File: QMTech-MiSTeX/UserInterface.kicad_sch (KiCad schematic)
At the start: 38 parts, among them CN2 U.FL-R-SMT-1(80), CN3 U.FL-R-SMT-1(80), CN4 U.FL-R-SMT-1(80), SW1 TS-1187A-B-A-B, SW2 TS-1187A-B-A-B, SW3 TS-1187A-B-A-B, SW4 TS-1187A-B-A-B, U6 HX 0.5-24P XGXJ-H2.0

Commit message: QMTech-MiSTeX WIP
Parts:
- removed U6: HX 0.5-24P XGXJ-H2.0, easyeda2kicad:CONN-SMD_24P-P0.50_HANXIA_HX0.5-24PXGXJ-H2.0, symbol easyeda2kicad:HX0.5-24PXGXJ-H2.0
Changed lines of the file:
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@@
-    )
-  )
-  (symbol (lib_id "easyeda2kicad:HX0.5-24PXGXJ-H2.0") (at 148.2598 107.5182 0) (unit 1)
-    (in_bom yes) (on_board yes) (dnp no) (fields_autoplaced)
-    (property "Reference" "U6" (at 156.5148 105.0361 0)
-      (effects (font (size 1.27 1.27)) (justify left))
-    )
-    (property "Value" "HX 0.5-24P XGXJ-H2.0" (at 156.5148 107.4603 0)
-      (effects (font (size 1.27 1.27)) (justify left))
-    )
-    (property "Footprint" "easyeda2kicad:CONN-SMD_24P-P0.50_HANXIA_HX0.5-24PXGXJ-H2.0" (at 148.2598 148.1582 0)
-      (effects (font (size 1.27 1.27)) hide)
-    )
-    (property "Datasheet" "" (at 148.2598 107.5182 0)
-      (effects (font (size 1.27 1.27)) hide)
-    )
-    (property "LCSC Part" "C5142050" (at 148.2598 150.6982 0)
-      (effects (font (size 1.27 1.27)) hide)
-    )
-    (pin "3")
-    (pin "26")
-    (pin "24")
-    (pin "8")
-    (pin "4")
-    (pin "7")
-    (pin "15")
-    (pin "14")
-    (pin "12")
-    (pin "13")
-    (pin "11")
-    (pin "6")
-    (pin "19")
-    (pin "9")
-    (pin "1")
-    (pin "10")
-    (pin "2")
-    (pin "22")
-    (pin "16")
-    (pin "21")
-    (pin "18")
-    (pin "20")
-    (pin "5")
-    (pin "23")
-    (pin "17")
-    (pin "25")
-    (instances
-      (project "QMTech-MiSTeX"
-        (path "/bf95850e-2fcb-4784-a603-f17fc357556b/cce2b405-ae09-44af-ba42-d113d6ffe521"
-          (reference "U6") (unit 1)
-        )
-      )
     )
   )

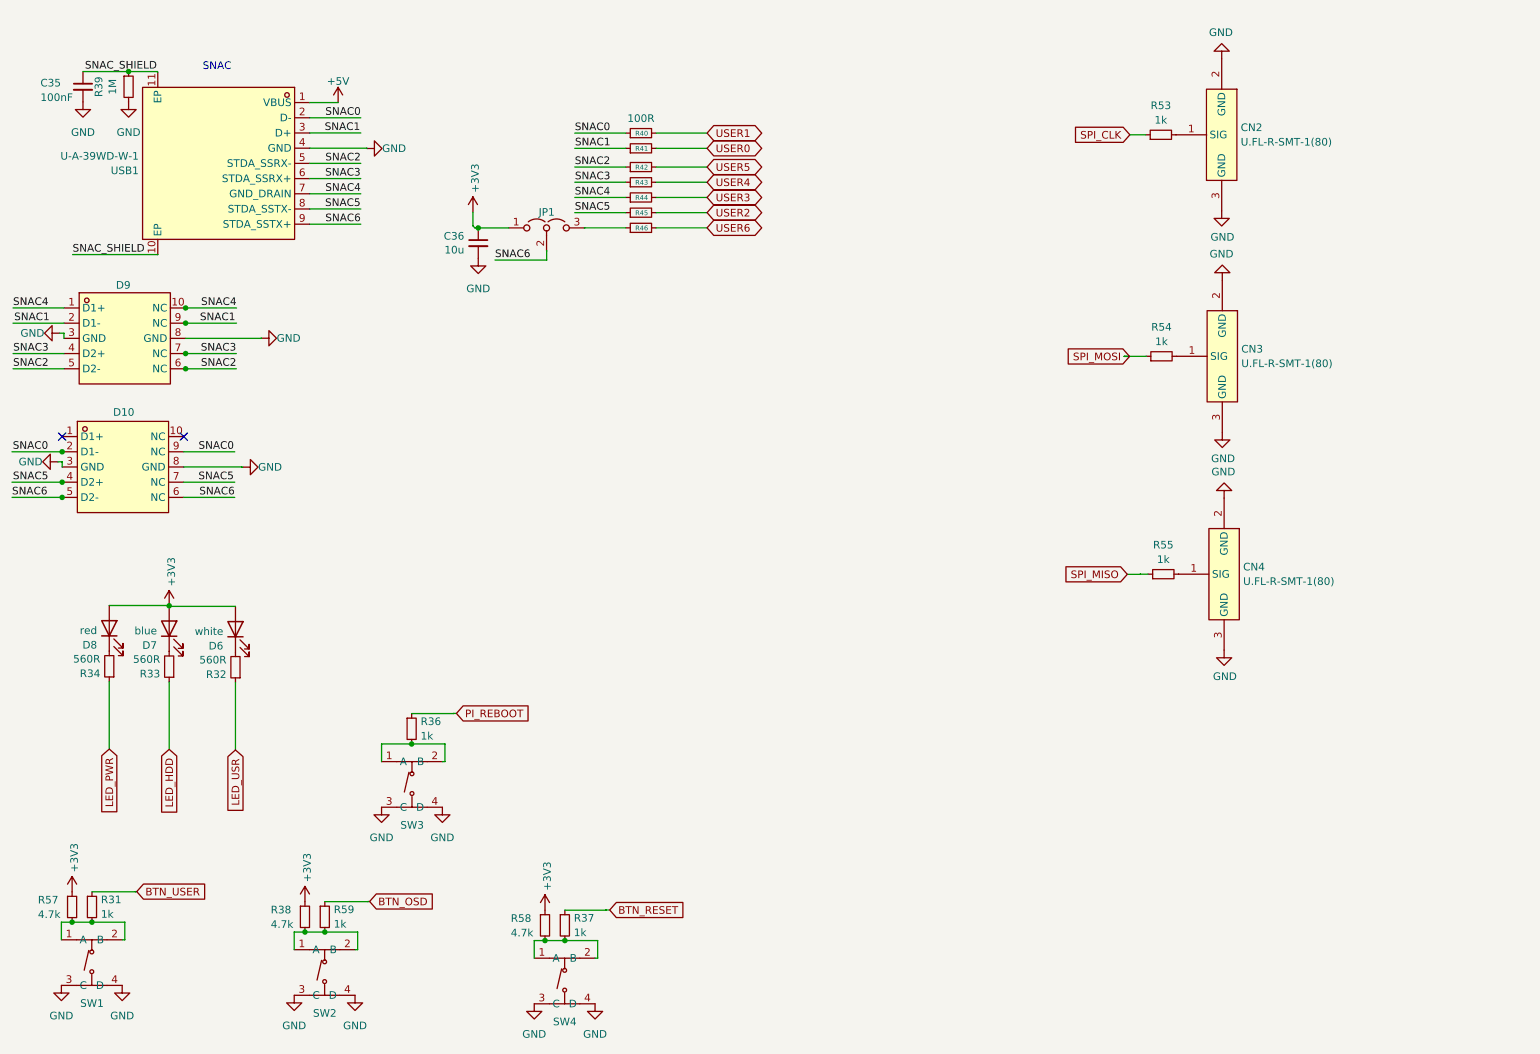
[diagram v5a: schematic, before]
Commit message: power filtering, testpoints, bottom caps, more decoupling, teardrops
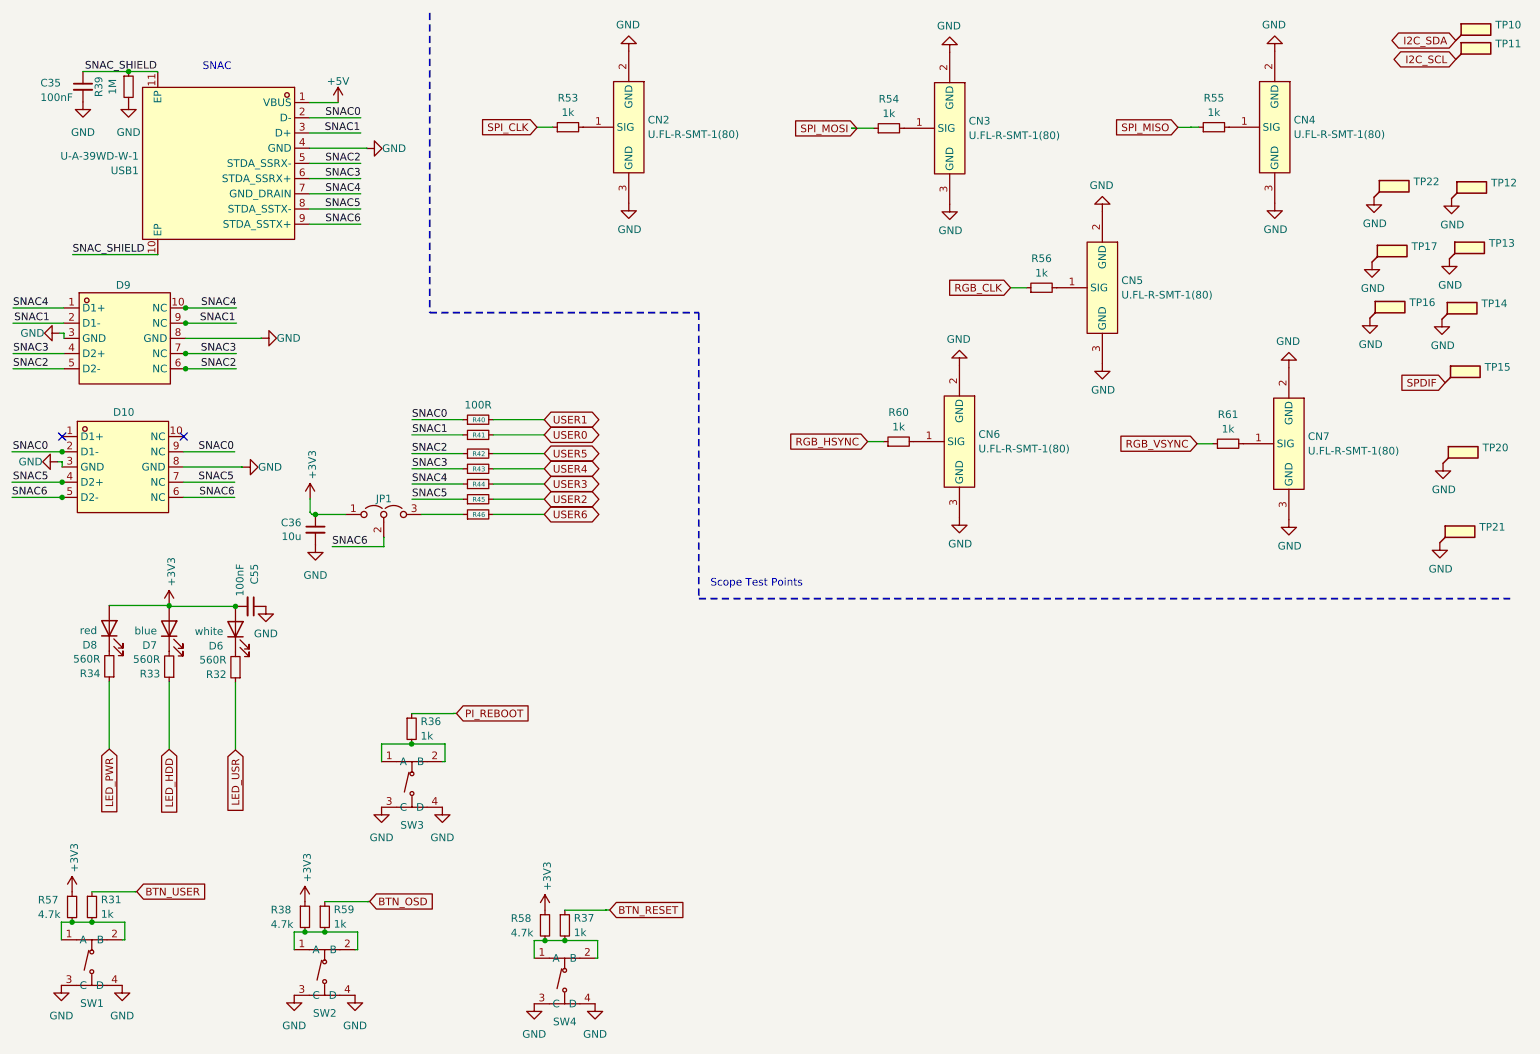
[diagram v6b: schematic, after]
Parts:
- added C55: 100nF, C_0402_1005Metric, symbol jlcpcb-basic-mlcc-0402:100nF
- added CN5, CN6, CN7: U.FL-R-SMT-1(80), easyeda2kicad:RF-SMD_FRF05002-JSS103M, symbol easyeda2kicad:U.FL-R-SMT-1(80)
- added R56, R60, R61: 1k, R_0402_1005Metric, symbol jlcpcb-basic-resistor-0402:1k
- added TP10, TP11, TP12, TP13, TP14, TP15, TP16, TP17, TP20, TP21, TP22: TestPoint_Flag, TestPoint:TestPoint_Pad_D1.5mm, symbol Connector:TestPoint_Flag
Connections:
- net +3V3: now also C55.2
- net GND: now also C55.1, CN5.2 (GND), CN5.3 (GND), CN6.2 (GND), CN6.3 (GND), CN7.2 (GND), CN7.3 (GND), TP12.1, TP13.1, TP14.1, TP16.1, TP17.1, TP20.1, TP21.1, TP22.1
- new net: CN5.1 (SIG), R56.2
- new net: CN7.1 (SIG), R61.2
- new net: CN6.1 (SIG), R60.2
- new net I2C_SCL: TP11.1
- new net I2C_SDA: TP10.1
- new net RGB_CLK: R56.1
- new net RGB_HSYNC: R60.1
- new net RGB_VSYNC: R61.1
- new net SPDIF: TP15.1
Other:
- note added: "Scope Test Points"
- title: (none) -> User and Test Interface
- moved on the sheet: C36, CN2, CN3, CN4, JP1, R40, R41, R42, R43, R44, R45, R46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

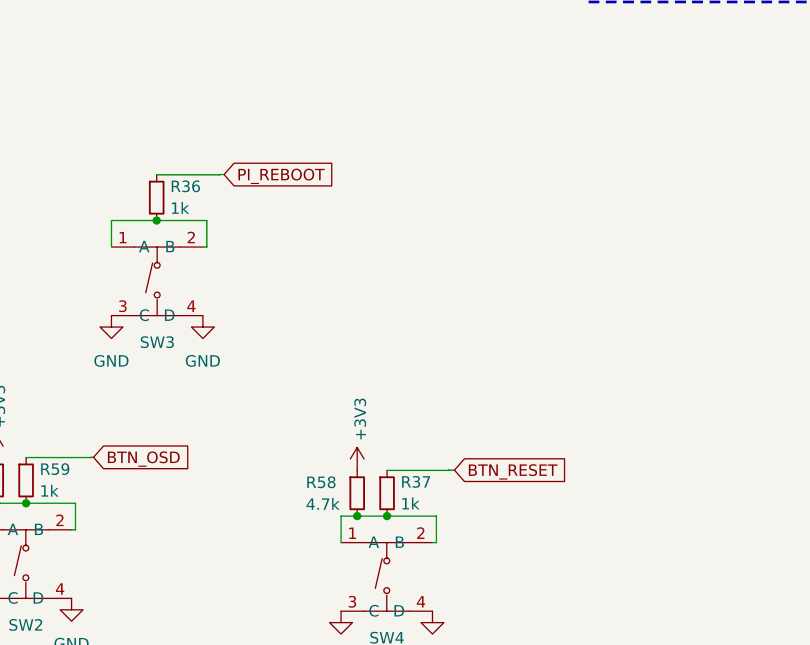
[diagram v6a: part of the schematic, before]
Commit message: connect buttons to the HPS, not the FPGA, because the FPGA does not use them
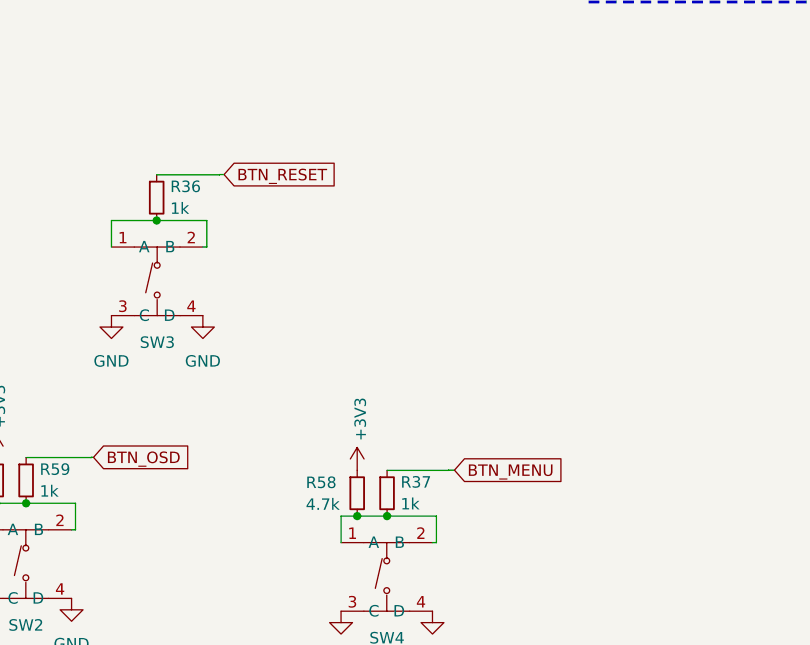
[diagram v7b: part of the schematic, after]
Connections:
- net PI_REBOOT is gone; now on net BTN_RESET: R36.1
- net BTN_RESET: no longer R37.1
- new net BTN_MENU: R37.1
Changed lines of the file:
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@@
     )
   )
-  (global_label "BTN_RESET" (shape input) (at 126.5557 167.3352 0) (fields_autoplaced)
+  (global_label "BTN_RESET" (shape input) (at 100.9566 134.493 0) (fields_autoplaced)
     (effects (font (size 1.27 1.27)) (justify left))
-    (property "Intersheetrefs" "${INTERSHEET_REFS}" (at 139.8217 167.3352 0)
+    (property "Intersheetrefs" "${INTERSHEET_REFS}" (at 114.2226 134.493 0)
       (effects (font (size 1.27 1.27)) (justify left))
     )
@@
     )
   )
-  (global_label "PI_REBOOT" (shape input) (at 100.9566 134.493 0) (fields_autoplaced)
+  (global_label "BTN_MENU" (shape input) (at 126.5557 167.3352 0) (fields_autoplaced)
     (effects (font (size 1.27 1.27)) (justify left))
-    (property "Intersheetrefs" "${INTERSHEET_REFS}" (at 114.1018 134.493 0)
+    (property "Intersheetrefs" "${INTERSHEET_REFS}" (at 139.4331 167.3352 0)
       (effects (font (size 1.27 1.27)) (justify left))
     )
